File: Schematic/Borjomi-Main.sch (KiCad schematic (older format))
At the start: 14 parts, among them J1 Vin 12V, J2 Gate 220V, J3 Vout 12V, J4 Data, J5 Pressure, U1 CAN_Module, U2 CurrentMeas_12V, U3 Relay_12Vout, U4 Relay_Gate220V, U5 Bluetooth

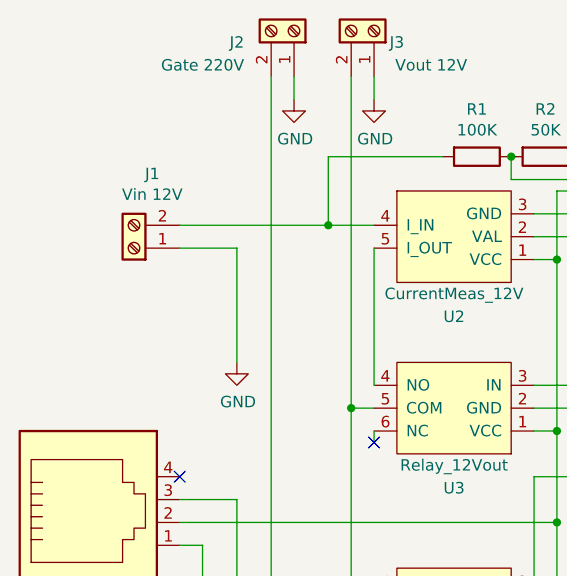
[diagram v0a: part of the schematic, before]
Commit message: Update schematics/pcb to use barrel_connector as 12V IN
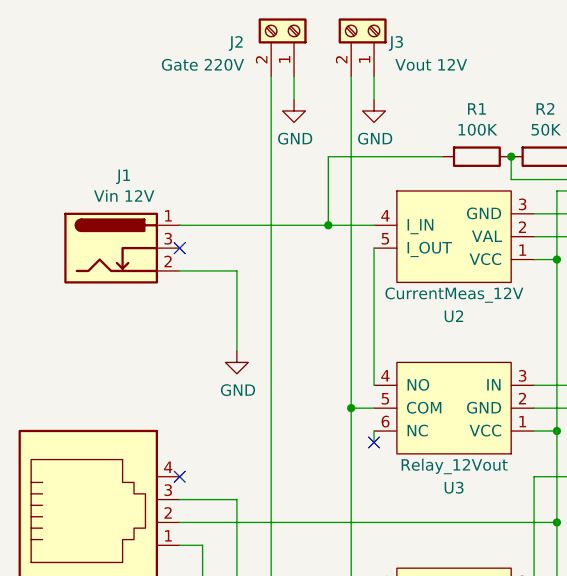
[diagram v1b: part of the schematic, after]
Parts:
- removed J1: Vin 12V, Connector:Degson_DG301_1x02_P5.00mm_Horizontal, symbol Connector:Screw_Terminal_01x02
- added J1: Vin 12V, Connector_BarrelJack:BarrelJack_Horizontal, symbol Connector:Barrel_Jack_Switch
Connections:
- net GND: now also J1.2
- net at R1.2, U2.4 (I_IN): now also J1.1
- no-connect marks 20 -> 21
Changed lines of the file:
@@
 	5800 1450 3850 1450
-$Comp
-L Connector:Screw_Terminal_01x02 J1
-U 1 1 5B6F66B3
-P 1550 1850
-F 0 "J1" H 1470 1525 50  0000 C CNN
-F 1 "Vin 12V" H 1470 1616 50  0000 C CNN
-F 2 "Connector:Degson_DG301_1x02_P5.00mm_Horizontal" H 1550 1850 50  0001 C CNN
-F 3 "~" H 1550 1850 50  0001 C CNN
-	1    1550 1850
-	-1   0    0    1
-$EndComp
 $Comp
 L power:GND #PWR04
@@
 L power:GND #PWR01
 U 1 1 5B6F704F
-P 2000 2350
-F 0 "#PWR01" H 2000 2100 50  0001 C CNN
-F 1 "GND" H 2005 2177 50  0000 C CNN
-F 2 "" H 2000 2350 50  0001 C CNN
-F 3 "" H 2000 2350 50  0001 C CNN
-	1    2000 2350
-	1    0    0    -1
-$EndComp
-Wire Wire Line
-	1750 1850 2000 1850
+P 2000 2300
+F 0 "#PWR01" H 2000 2050 50  0001 C CNN
+F 1 "GND" H 2005 2127 50  0000 C CNN
+F 2 "" H 2000 2300 50  0001 C CNN
+F 3 "" H 2000 2300 50  0001 C CNN
+	1    2000 2300
+	1    0    0    -1
+$EndComp
+Wire Wire Line
+	1750 1950 2000 1950
 $Comp
 L Connector:RJ14 J4
@@
 	3300 2850 3300 3350
 Wire Wire Line
-	2000 2350 2000 1850
-Wire Wire Line
 	2600 1100 2600 1200
 Wire Wire Line
@@
 	-1   0    0    1
 $EndComp
+$Comp
+L Connector:Barrel_Jack_Switch J1
+U 1 1 5D0EB08D
+P 1450 1850
+F 0 "J1" H 1507 2167 50  0000 C CNN
+F 1 "Vin 12V" H 1507 2076 50  0000 C CNN
+F 2 "Connector_BarrelJack:BarrelJack_Horizontal" H 1500 1810 50  0001 C CNN
+F 3 "~" H 1500 1810 50  0001 C CNN
+	1    1450 1850
+	1    0    0    -1
+$EndComp
+Wire Wire Line
+	2000 1950 2000 2300
+NoConn ~ 1750 1850
 $EndSCHEMATC

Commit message: Board Borjomi-Main v1.1 with Gerber/Drill files
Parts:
- added J6: LaptopSwitch, Connector:RJ14_YH-57-21_5722_6P4C, symbol Connector:RJ14
- added JP1: Jumper, Connector:SimpleJumper_Pitch5.08mm_Drill0.7mm_2pad, symbol Device:Jumper
- added U6: Relay_LaptopSwitch, RelayModule:Relay_Module_1_Channel_Holes0.9, symbol RelayModule:5V_1_Channel_Relay_Module
- A1: symbol MCU_Module:Arduino_Nano_v3.x -> Borjomi-Main-rescue:Arduino_Nano_v3.x-MCU_Module
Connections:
- net GND: now also U6.2 (GND)
- net at A1.11 (D8): now also JP1.2
- net at A1.27 (+5V), J5.2, U1.9 (VCC)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: now also U6.1 (VCC)
- new net: J6.2, U6.5 (COM)
- new net: J6.3, U6.4 (NO)
- new net: JP1.1, U6.3 (IN)
- no-connect marks 21 -> 23
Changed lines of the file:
@@
 EESchema Schematic File Version 4
-LIBS:Borjomi-Main-cache
-EELAYER 29 0
+EELAYER 30 0
 EELAYER END
 $Descr A4 11693 8268
@@
 $EndDescr
 $Comp
-L MCU_Module:Arduino_Nano_v3.x A1
+L Borjomi-Main-rescue:Arduino_Nano_v3.x-MCU_Module A1
 U 1 1 5B6D71E4
 P 4550 2750
@@
 	5800 2100 5800 1450
 Wire Wire Line
-	5800 1450 3850 1450
+	5800 1450 3900 1450
 $Comp
 L power:GND #PWR04
@@
 	1750 4200 1950 4200
 Wire Wire Line
-	1950 4200 1950 4750
-Wire Wire Line
 	8200 2600 8200 4650
-Wire Wire Line
-	1900 4650 8200 4650
 $Comp
 L power:GND #PWR03
 U 1 1 5B7075AE
-P 3500 3900
-F 0 "#PWR03" H 3500 3650 50  0001 C CNN
-F 1 "GND" H 3505 3727 50  0000 C CNN
-F 2 "" H 3500 3900 50  0001 C CNN
-F 3 "" H 3500 3900 50  0001 C CNN
-	1    3500 3900
+P 3500 5650
+F 0 "#PWR03" H 3500 5400 50  0001 C CNN
+F 1 "GND" H 3505 5477 50  0000 C CNN
+F 2 "" H 3500 5650 50  0001 C CNN
+F 3 "" H 3500 5650 50  0001 C CNN
+	1    3500 5650
 	1    0    0    -1
 $EndComp
@@
 NoConn ~ 4050 2250
 NoConn ~ 4050 2750
-NoConn ~ 4050 2950
 NoConn ~ 5050 3450
 NoConn ~ 5050 3350
@@
 	8200 2500 8300 2500
 Wire Wire Line
-	1950 4750 8300 4750
-Wire Wire Line
-	3850 2650 4050 2650
-Wire Wire Line
-	3850 1450 3850 2650
+	3900 1450 3900 2650
 $Comp
 L Diode:1N5408 D1
@@
 Connection ~ 4750 1600
 Wire Wire Line
-	6050 1050 3950 1050
-Wire Wire Line
-	3950 1050 3950 2550
-Wire Wire Line
-	3950 2550 4050 2550
-Wire Wire Line
-	4050 3150 3750 3150
-Wire Wire Line
-	3750 3150 3750 1150
-Wire Wire Line
-	3750 1150 6050 1150
+	6050 1050 4000 1050
+Wire Wire Line
+	4000 1050 4000 2550
+Wire Wire Line
+	3700 3150 3700 1150
 NoConn ~ 6750 900
 NoConn ~ 6750 1100
@@
 	1850 3150 1850 3400
 Wire Wire Line
-	3500 3450 3500 3900
+	3500 3450 3500 5250
 Connection ~ 3500 3450
 Wire Wire Line
@@
 	2000 2950 2000 4150
 Wire Wire Line
-	2000 4150 5550 4150
-Wire Wire Line
-	5550 4150 5550 3150
-Wire Wire Line
-	5550 3150 5050 3150
+	2000 4150 5500 4150
+Wire Wire Line
+	5500 4150 5500 3150
 NoConn ~ 1750 2850
 $Comp
@@
 	2000 1950 2000 2300
 NoConn ~ 1750 1850
+Wire Wire Line
+	1950 4200 1950 4750
+Wire Wire Line
+	1950 4750 8300 4750
+Wire Wire Line
+	1900 4650 8200 4650
+NoConn ~ 1750 5050
+NoConn ~ 1750 5350
+$Comp
+L RelayModule:5V_1_Channel_Relay_Module U6
+U 1 1 5F4B5258
+P 2950 5250
+F 0 "U6" H 2950 5600 50  0000 C CNN
+F 1 "Relay_LaptopSwitch" H 2950 5500 50  0000 C CNN
+F 2 "RelayModule:Relay_Module_1_Channel_Holes0.9" H 2950 5250 50  0001 C CNN
+F 3 "" H 2950 5250 50  0001 C CNN
+	1    2950 5250
+	-1   0    0    1
+$EndComp
+Wire Wire Line
+	3400 3550 3400 5350
+Wire Wire Line
+	3400 5350 3300 5350
+Connection ~ 3400 3550
+Wire Wire Line
+	3300 5250 3500 5250
+Connection ~ 3500 5250
+Wire Wire Line
+	3500 5250 3500 5650
+Wire Wire Line
+	4050 3150 3700 3150
+Wire Wire Line
+	3700 1150 6050 1150
+Wire Wire Line
+	4000 2550 4050 2550
+Wire Wire Line
+	3900 2650 4050 2650
+Wire Wire Line
+	4050 2950 3800 2950
+Wire Wire Line
+	3800 2950 3800 1300
+Wire Wire Line
+	3800 1300 5650 1300
+Wire Wire Line
+	5650 1300 5650 5150
+Wire Wire Line
+	5500 3150 5050 3150
+NoConn ~ 2600 5350
+$Comp
+L Connector:RJ14 J6
+U 1 1 5F4A4CD0
+P 1350 5250
+F 0 "J6" H 1100 4900 50  0000 C CNN
+F 1 "LaptopSwitch" H 1550 4900 50  0000 C CNN
+F 2 "Connector:RJ14_YH-57-21_5722_6P4C" H 1350 5250 50  0001 C CNN
+F 3 "https://www.rcscomponents.kiev.ua/product/rozetka-yh-57-21-5722-6p4c_12940.html" H 1350 5250 50  0001 C CNN
+	1    1350 5250
+	1    0    0    -1
+$EndComp
+Wire Wire Line
+	1750 5150 2600 5150
+Wire Wire Line
+	1750 5250 2600 5250
+$Comp
+L Device:Jumper JP1
+U 1 1 5F4B8C4C
+P 4550 5150
+F 0 "JP1" H 4550 5414 50  0000 C CNN
+F 1 "Jumper" H 4550 5323 50  0000 C CNN
+F 2 "Connector:SimpleJumper_Pitch5.08mm_Drill0.7mm_2pad" H 4550 5150 50  0001 C CNN
+F 3 "~" H 4550 5150 50  0001 C CNN
+	1    4550 5150
+	1    0    0    -1
+$EndComp
+Wire Wire Line
+	3300 5150 4250 5150
+Wire Wire Line
+	4850 5150 5650 5150
 $EndSCHEMATC
